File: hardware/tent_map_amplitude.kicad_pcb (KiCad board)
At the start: 4 copper layers, 56.4 x 60.2 mm, 57 parts, among them U1 LM339AN, U2 TL082IP, U3 TL082IP, U4 LF398_DIP8, U5 LF398_DIP8, U6 LF398_DIP8

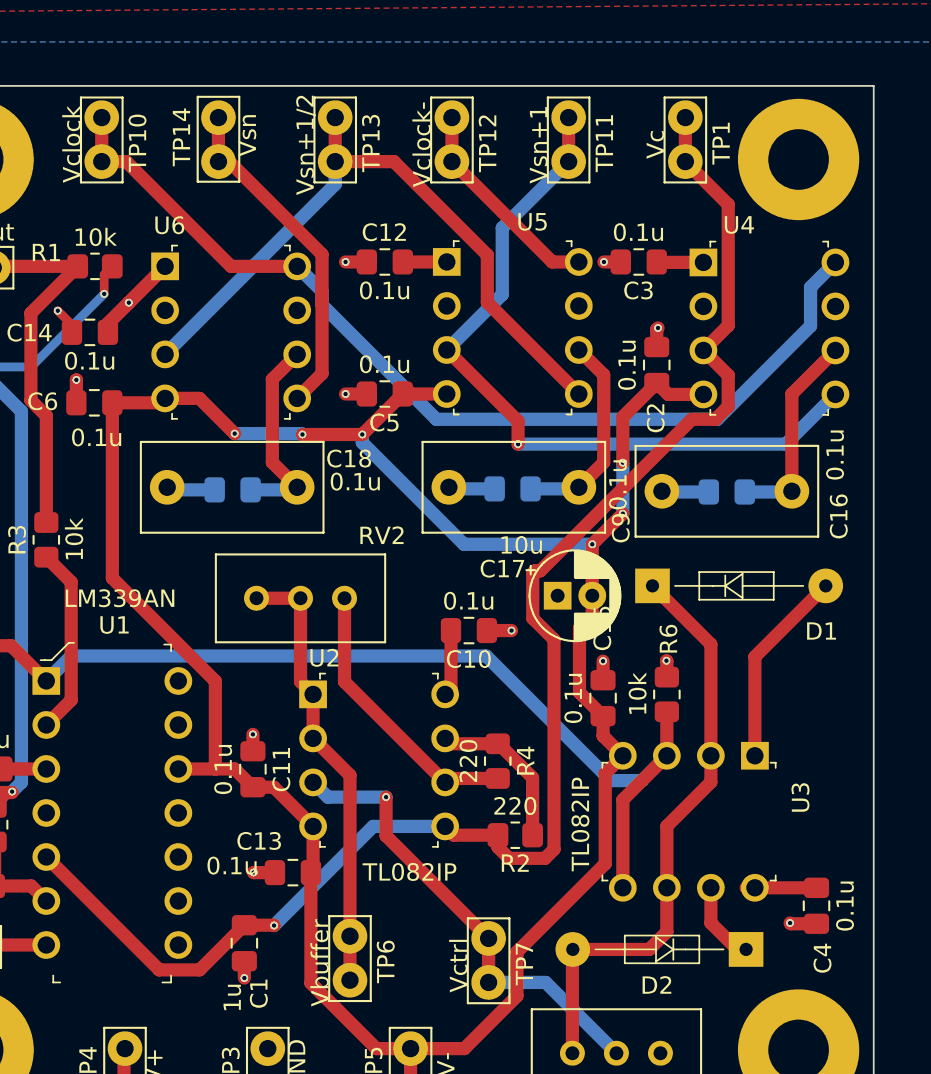
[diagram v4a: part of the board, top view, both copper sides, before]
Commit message: Add stitching vias to fill in ground planes on top and bottom copper
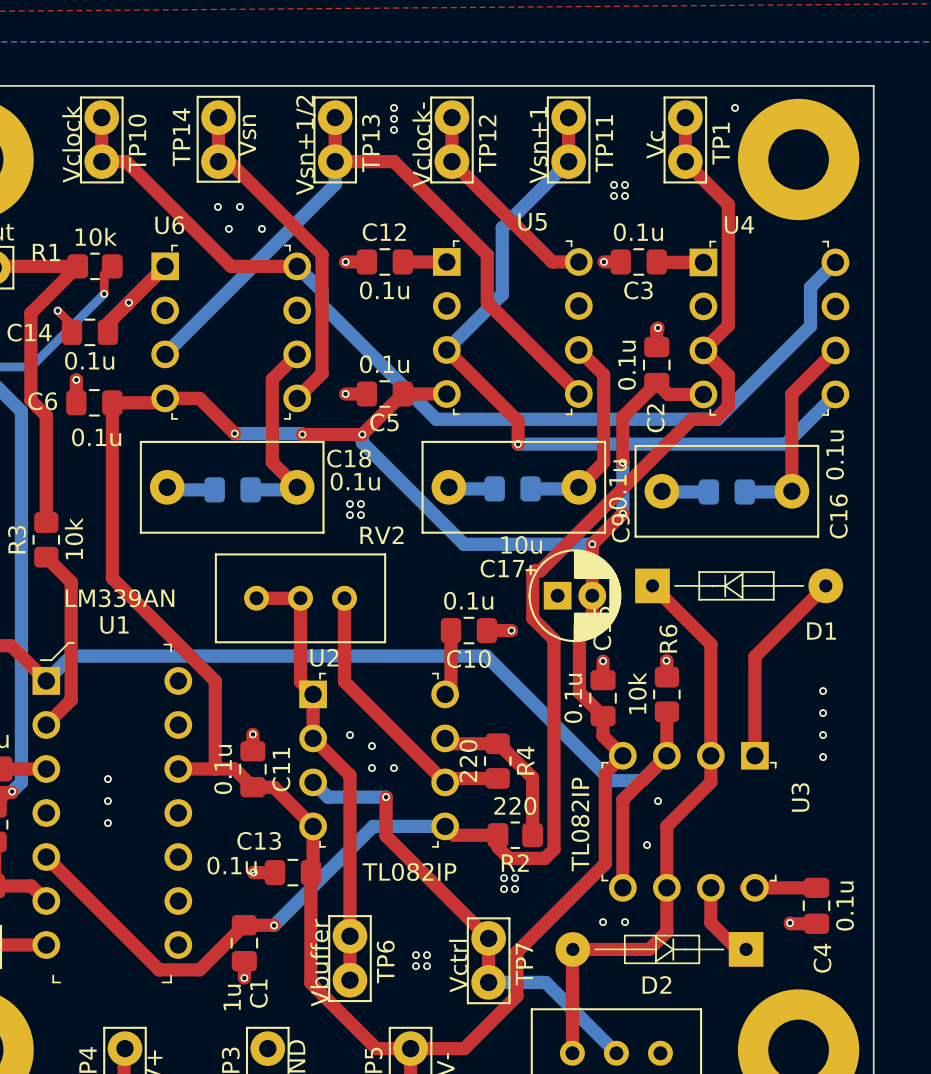
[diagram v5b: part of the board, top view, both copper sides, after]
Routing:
- net GND: vias 14 -> 53
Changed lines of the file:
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@@
     (thickness 1.6002)
     (drawings 5)
-    (tracks 268)
+    (tracks 307)
     (zones 0)
     (modules 57)
@@
   (segment (start 110.4138 67.3862) (end 110.49 67.31) (width 0.762) (layer Front) (net 1))
   (segment (start 110.4138 68.41) (end 110.4138 67.3862) (width 0.762) (layer Front) (net 1))
+  (via (at 96.52 103.505) (size 0.4572) (drill 0.254) (layers Front Back) (net 1))
+  (via (at 96.52 104.14) (size 0.4572) (drill 0.254) (layers Front Back) (net 1))
+  (via (at 97.155 104.14) (size 0.4572) (drill 0.254) (layers Front Back) (net 1))
+  (via (at 97.155 103.505) (size 0.4572) (drill 0.254) (layers Front Back) (net 1))
+  (via (at 101.6 99.06) (size 0.4572) (drill 0.254) (layers Front Back) (net 1))
+  (via (at 102.235 99.06) (size 0.4572) (drill 0.254) (layers Front Back) (net 1))
+  (via (at 102.235 99.695) (size 0.4572) (drill 0.254) (layers Front Back) (net 1))
+  (via (at 101.6 99.695) (size 0.4572) (drill 0.254) (layers Front Back) (net 1))
+  (via (at 92.71 77.47) (size 0.4572) (drill 0.254) (layers Front Back) (net 1))
+  (via (at 93.345 77.47) (size 0.4572) (drill 0.254) (layers Front Back) (net 1))
+  (via (at 93.345 78.105) (size 0.4572) (drill 0.254) (layers Front Back) (net 1))
+  (via (at 92.71 78.105) (size 0.4572) (drill 0.254) (layers Front Back) (net 1))
+  (via (at 107.95 59.055) (size 0.4572) (drill 0.254) (layers Front Back) (net 1))
+  (via (at 108.585 59.055) (size 0.4572) (drill 0.254) (layers Front Back) (net 1))
+  (via (at 108.585 59.69) (size 0.4572) (drill 0.254) (layers Front Back) (net 1))
+  (via (at 107.95 59.69) (size 0.4572) (drill 0.254) (layers Front Back) (net 1))
+  (via (at 95.25 54.61) (size 0.4572) (drill 0.254) (layers Front Back) (net 1))
+  (via (at 95.25 55.245) (size 0.4572) (drill 0.254) (layers Front Back) (net 1))
+  (via (at 95.25 55.88) (size 0.4572) (drill 0.254) (layers Front Back) (net 1))
+  (via (at 85.09 60.325) (size 0.4572) (drill 0.254) (layers Front Back) (net 1))
+  (via (at 86.36 60.325) (size 0.4572) (drill 0.254) (layers Front Back) (net 1))
+  (via (at 85.725 61.595) (size 0.4572) (drill 0.254) (layers Front Back) (net 1))
+  (via (at 87.63 61.595) (size 0.4572) (drill 0.254) (layers Front Back) (net 1))
+  (via (at 109.855 97.155) (size 0.4572) (drill 0.254) (layers Front Back) (net 1))
+  (via (at 110.49 94.615) (size 0.4572) (drill 0.254) (layers Front Back) (net 1))
+  (via (at 107.315 101.6) (size 0.4572) (drill 0.254) (layers Front Back) (net 1))
+  (via (at 108.585 101.6) (size 0.4572) (drill 0.254) (layers Front Back) (net 1))
+  (via (at 120.015 92.075) (size 0.4572) (drill 0.254) (layers Front Back) (net 1))
+  (via (at 120.015 90.805) (size 0.4572) (drill 0.254) (layers Front Back) (net 1))
+  (via (at 120.015 89.535) (size 0.4572) (drill 0.254) (layers Front Back) (net 1))
+  (via (at 120.015 88.265) (size 0.4572) (drill 0.254) (layers Front Back) (net 1))
+  (via (at 78.74 95.885) (size 0.4572) (drill 0.254) (layers Front Back) (net 1))
+  (via (at 78.74 94.615) (size 0.4572) (drill 0.254) (layers Front Back) (net 1))
+  (via (at 78.74 93.345) (size 0.4572) (drill 0.254) (layers Front Back) (net 1))
+  (via (at 93.98 91.44) (size 0.4572) (drill 0.254) (layers Front Back) (net 1))
+  (via (at 93.98 92.71) (size 0.4572) (drill 0.254) (layers Front Back) (net 1))
+  (via (at 95.25 92.71) (size 0.4572) (drill 0.254) (layers Front Back) (net 1))
+  (via (at 92.71 90.805) (size 0.4572) (drill 0.254) (layers Front Back) (net 1))
+  (via (at 114.935 54.61) (size 0.4572) (drill 0.254) (layers Front Back) (net 1))
   (segment (start 98.70948 96.5835) (end 98.20148 96.0755) (width 0.762) (layer Front) (net 2))
   (segment (start 101.24948 96.5835) (end 98.70948 96.5835) (width 0.762) (layer Front) (net 2))

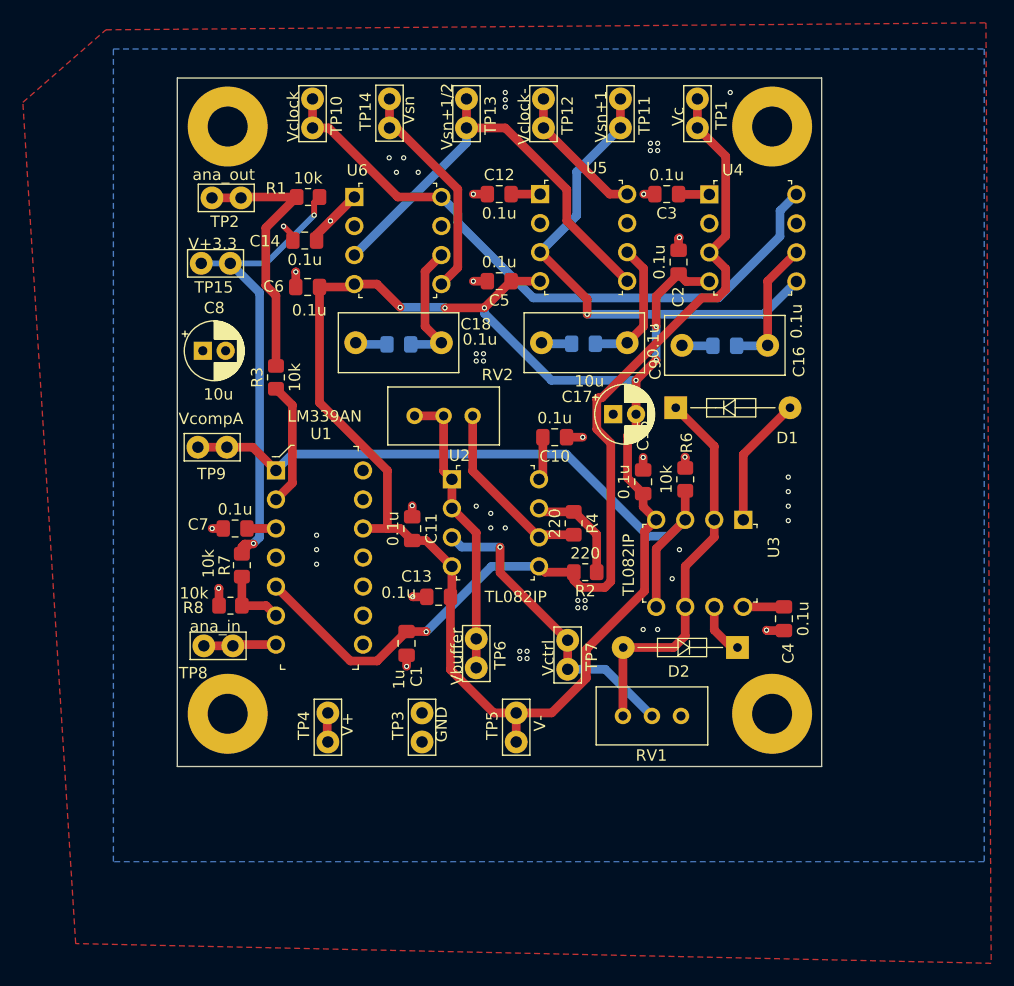
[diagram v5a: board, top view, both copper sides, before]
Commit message: Add rounded board edges, move edges out to strengthen holes
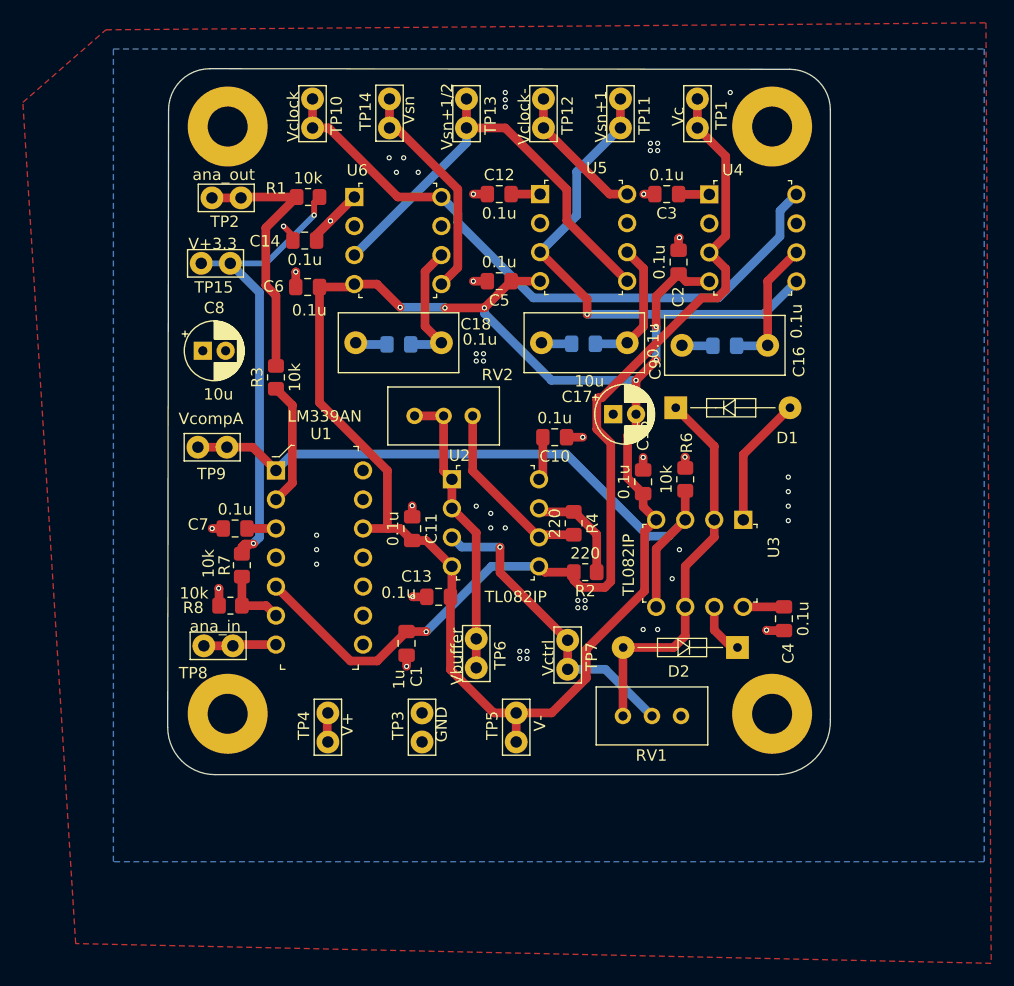
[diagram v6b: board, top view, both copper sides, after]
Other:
- board size 56.4 x 60.2 mm -> 58 x 61.8 mm
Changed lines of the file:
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@@
   (general
     (thickness 1.6002)
-    (drawings 5)
+    (drawings 10)
     (tracks 307)
     (zones 0)
@@
     )
   )
-  (gr_line (start 122.936 53.34) (end 122.936 113.5888) (layer Edge.Cuts) (width 0.1))
-  (gr_line (start 66.548 53.34) (end 122.936 53.34) (layer Edge.Cuts) (width 0.1))
-  (gr_line (start 66.548 113.5888) (end 66.548 53.34) (layer Edge.Cuts) (width 0.1))
-  (gr_line (start 122.936 113.5888) (end 66.548 113.5888) (layer Edge.Cuts) (width 0.1))
+  (gr_arc (start 120.141638 56.134) (end 123.698 56.134) (angle -90) (layer Edge.Cuts) (width 0.0381))
+  (gr_arc (start 69.3928 56.134) (end 69.3928 52.5272) (angle -90) (layer Edge.Cuts) (width 0.0381))
+  (gr_arc (start 69.85 110.1598) (end 65.7098 110.1598) (angle -90) (layer Edge.Cuts) (width 0.0381))
+  (gr_arc (start 119.024401 109.626401) (end 119.126 114.3) (angle -90.29447402) (layer Edge.Cuts) (width 0.0381))
+  (gr_arc (start 118.7196 113.5888) (end 122.936 113.5888) (angle -334.2495259) (layer Cmts.User) (width 0.15))
+  (gr_line (start 123.698 56.134) (end 123.697416 109.500783) (layer Edge.Cuts) (width 0.1))
+  (gr_line (start 69.3928 52.5272) (end 120.141638 52.577638) (layer Edge.Cuts) (width 0.1))
+  (gr_line (start 65.7098 110.1598) (end 65.786 56.134) (layer Edge.Cuts) (width 0.1))
+  (gr_line (start 119.126 114.3) (end 69.85 114.3) (layer Edge.Cuts) (width 0.1))
   (gr_text "Chaotic Crew\nsenior design 2020\ntent map CRNG" (at 112.0648 87.0712) (layer B.SilkS)
     (effects (font (size 1.5 1.4) (thickness 0.127)) (justify mirror))
